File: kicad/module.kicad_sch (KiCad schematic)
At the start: 14 parts, among them J2 Conn_01x12, J3 Conn_01x10, J4 Conn_01x02, Q1 SI2302CDS, SW1 CNK_KMR2, U10 RioteeModule, U9 TS5A3166YZP

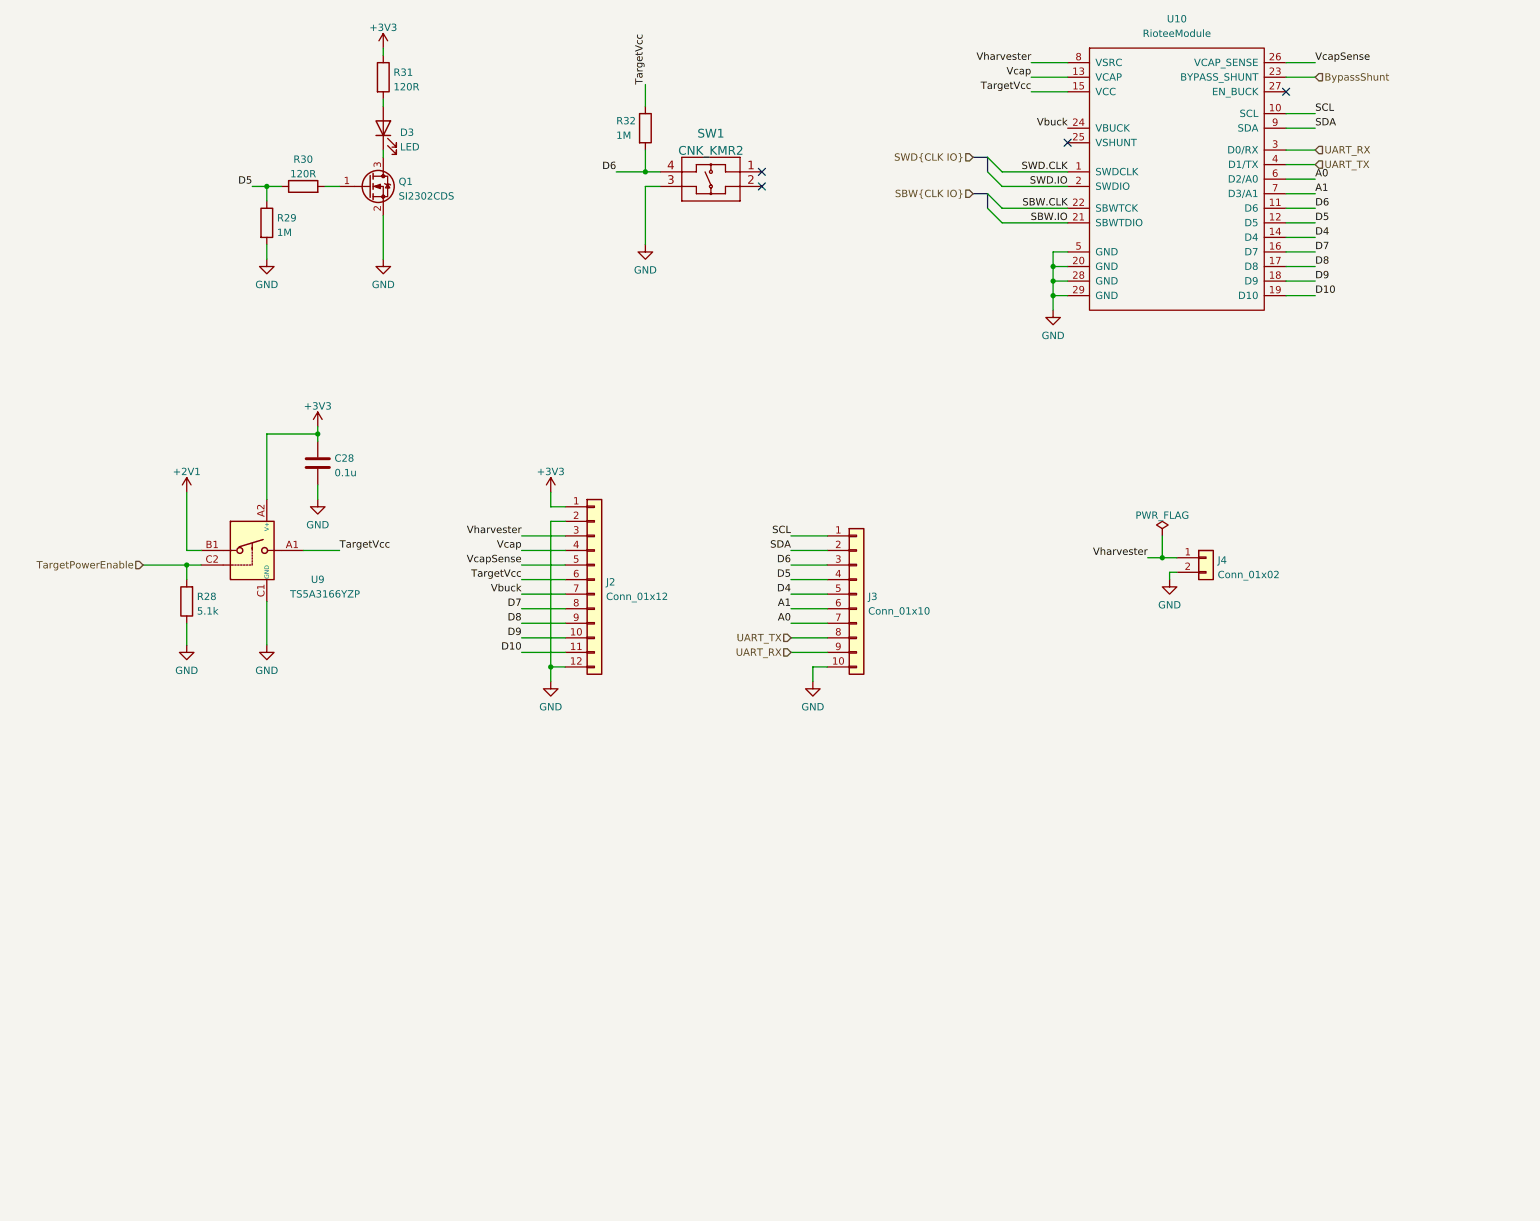
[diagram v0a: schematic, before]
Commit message: copy in module schematics
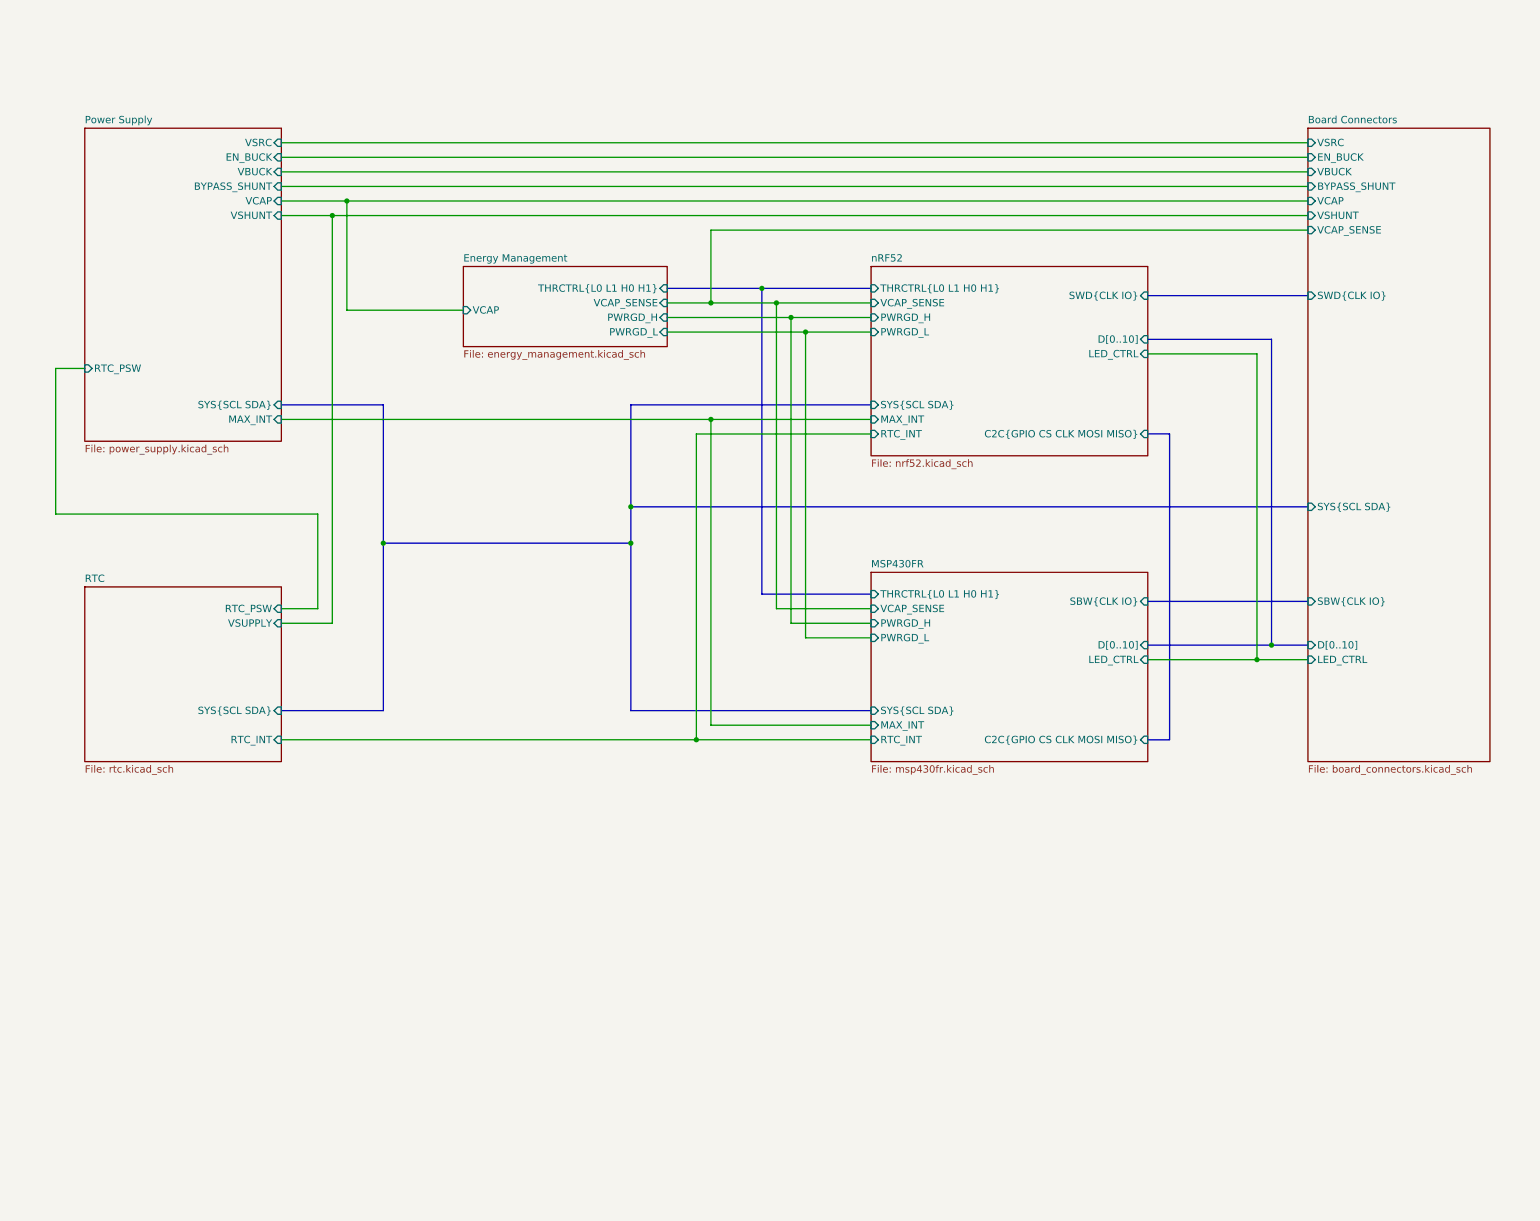
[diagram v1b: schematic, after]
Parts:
- removed C28: 0.1u, Capacitor_SMD:C_0402_1005Metric, symbol Device:C
- removed D3: LED, LED_SMD:LED_0402_1005Metric, symbol Device:LED
- removed J2: Conn_01x12, riotee:PinSocket_1x12_P2.54mm_Vertical, symbol Connector_Generic:Conn_01x12
- removed J3: Conn_01x10, riotee:PinSocket_1x10_P2.54mm_Vertical, symbol Connector_Generic:Conn_01x10
- removed J4: Conn_01x02, riotee:JST_S2B-PH-SM4-TB(LF)(SN), symbol Connector_Generic:Conn_01x02
- removed Q1: SI2302CDS, riotee:VSH_SOT-23-3, symbol riotee:SI2302CDS
- removed R28: 5.1k, Resistor_SMD:R_0402_1005Metric, symbol Device:R
- removed R29, R32: 1M, Resistor_SMD:R_0402_1005Metric, symbol Device:R
- removed R30, R31: 120R, Resistor_SMD:R_0402_1005Metric, symbol Device:R
- removed SW1: CNK_KMR2, riotee:CNK_KMR2_SW, symbol riotee:CNK_KMR2
- removed U10: RioteeModule, riotee:NC_RioteeModule, symbol riotee:RioteeModule
- removed U9: TS5A3166YZP, riotee:TI_YZP0005, symbol riotee:TS5A3166YZP
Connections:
- no-connect marks 4 -> 0
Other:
- added sheet Board Connectors (board_connectors.kicad_sch)
- added sheet Energy Management (energy_management.kicad_sch)
- added sheet MSP430FR (msp430fr.kicad_sch)
- added sheet Power Supply (power_supply.kicad_sch)
- added sheet RTC (rtc.kicad_sch)
- added sheet nRF52 (nrf52.kicad_sch)

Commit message: unify module and board
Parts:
- added D4: LED, Riotee:LED_0402_1005Metric, symbol Riotee:LED
- added J5: RFShield_OnePiece, Riotee:EMI_SHIELD_CSTM, symbol Device:RFShield_OnePiece
- added Q2: PMCM4401VNE, Riotee:NXP_WLCSP4, symbol Riotee:PMCM4401VNE
- added R33: 220k, Riotee:R_0201_0603Metric, symbol Riotee:R
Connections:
- new net: D4.1 (K), Q2.B1 (D)
- new net GND: J5.1 (Shield), Q2.A2 (S), R33.2
- new net LED_CTRL: Q2.A1 (G), R33.1
- new net VCC: D4.2 (A)
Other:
- removed sheet Board Connectors

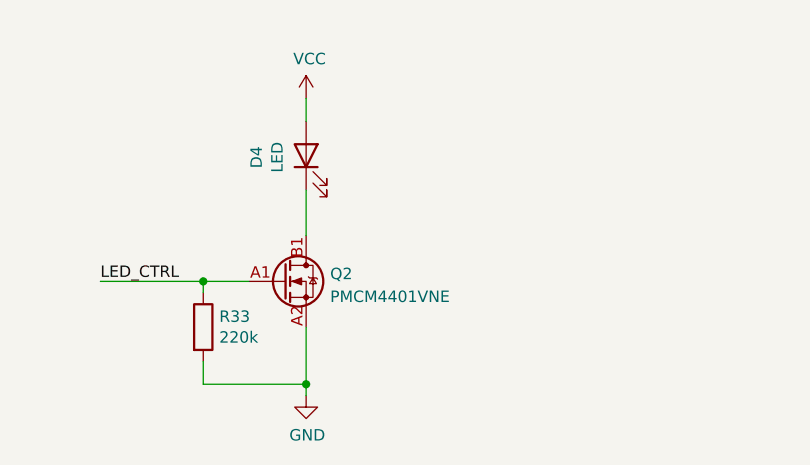
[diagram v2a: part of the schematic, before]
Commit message: move module parts to common library
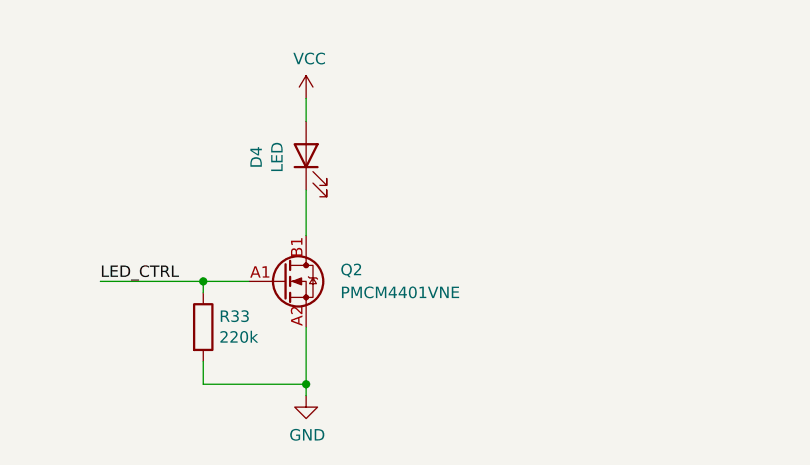
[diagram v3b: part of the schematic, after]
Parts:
- Q2: symbol Riotee:PMCM4401VNE -> riotee:PMCM4401VNE
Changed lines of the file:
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@@
 	)
 	(symbol
-		(lib_id "Riotee:PMCM4401VNE")
+		(lib_id "riotee:PMCM4401VNE")
 		(at 205.74 214.63 0)
 		(unit 1)
@@
 		(fields_autoplaced yes)
 		(property "Reference" "Q2"
-			(at 210.947 213.7953 0)
+			(at 212.09 213.3599 0)
 			(effects
 				(font
@@
 		)
 		(property "Value" "PMCM4401VNE"
-			(at 210.947 216.3322 0)
+			(at 212.09 215.8999 0)
 			(effects
 				(font
@@
 			)
 		)
-		(property "Description" "MOSFET N-CH 12V 4.7A 4WLCSP"
+		(property "Description" "N-MOSFET transistor"
 			(at 205.74 214.63 0)
 			(effects

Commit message: resolve ERC
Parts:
- D4: footprint Riotee:LED_0402_1005Metric -> riotee:LED_0402_1005Metric; symbol Riotee:LED -> Device:LED
- J5: footprint Riotee:EMI_SHIELD_CSTM -> riotee:EMI_SHIELD_CSTM
- Q2: footprint Riotee:NXP_WLCSP4 -> riotee:NXP_WLCSP4
- R33: footprint Riotee:R_0201_0603Metric -> riotee:R_0201_0603Metric; symbol Riotee:R -> Device:R
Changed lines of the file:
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@@
 	)
 	(symbol
-		(lib_id "Riotee:R")
+		(lib_id "Device:R")
 		(at 196.85 219.71 0)
 		(unit 1)
@@
 			)
 		)
-		(property "Footprint" "Riotee:R_0201_0603Metric"
+		(property "Footprint" "riotee:R_0201_0603Metric"
 			(at 195.072 219.71 90)
 			(effects
@@
 			)
 		)
-		(property "Description" "RES SMD 220K OHM 1% 1/20W 0201"
+		(property "Description" "Resistor"
 			(at 196.85 219.71 0)
 			(effects
@@
 	)
 	(symbol
-		(lib_id "Riotee:GND")
+		(lib_id "power:GND")
 		(at 124.46 223.52 0)
 		(unit 1)
@@
 			)
 		)
-		(property "Description" ""
+		(property "Description" "Power symbol creates a global label with name \"GND\" , ground"
 			(at 124.46 223.52 0)
 			(effects
@@
 			)
 		)
-		(property "Footprint" "Riotee:NXP_WLCSP4"
+		(property "Footprint" "riotee:NXP_WLCSP4"
 			(at 205.74 229.87 0)
 			(effects
@@
 	)
 	(symbol
-		(lib_id "Riotee:GND")
+		(lib_id "power:GND")
 		(at 208.28 227.33 0)
 		(unit 1)
@@
 			)
 		)
-		(property "Description" ""
+		(property "Description" "Power symbol creates a global label with name \"GND\" , ground"
 			(at 208.28 227.33 0)
 			(effects
@@
 			)
 		)
-		(property "Footprint" "Riotee:EMI_SHIELD_CSTM"
+		(property "Footprint" "riotee:EMI_SHIELD_CSTM"
 			(at 124.46 213.36 0)
 			(effects
@@
 	)
 	(symbol
-		(lib_id "Riotee:LED")
+		(lib_id "Device:LED")
 		(at 208.28 200.66 90)
 		(unit 1)
@@
 			)
 		)
-		(property "Footprint" "Riotee:LED_0402_1005Metric"
+		(property "Footprint" "riotee:LED_0402_1005Metric"
 			(at 208.28 200.66 0)
 			(effects
@@
 			)
 		)
-		(property "Description" "SMD LED 0402 RED 625NM"
+		(property "Description" "Light emitting diode"
 			(at 208.28 200.66 0)
 			(effects
@@
 			(at 208.28 200.66 0)
 			(effects
+				(font
+					(size 1.27 1.27)
+				)
+				(hide yes)
+			)
+		)
+		(property "Sim.Pins" "1=K 2=A"
+			(at 208.28 200.66 0)
+			(effects

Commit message: resolve remaining import errors
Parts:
- D4: footprint riotee:LED_0402_1005Metric -> LED_SMD:LED_0402_1005Metric
- J5: footprint riotee:EMI_SHIELD_CSTM -> riotee:MS209-20F
- R33: footprint riotee:R_0201_0603Metric -> Resistor_SMD:R_0201_0603Metric
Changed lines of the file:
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@@
 			)
 		)
-		(property "Footprint" "riotee:R_0201_0603Metric"
+		(property "Footprint" "Resistor_SMD:R_0201_0603Metric"
 			(at 195.072 219.71 90)
 			(effects
@@
 			)
 		)
-		(property "Footprint" "riotee:EMI_SHIELD_CSTM"
+		(property "Footprint" "riotee:MS209-20F"
 			(at 124.46 213.36 0)
 			(effects
@@
 			)
 		)
-		(property "Footprint" "riotee:LED_0402_1005Metric"
+		(property "Footprint" "LED_SMD:LED_0402_1005Metric"
 			(at 208.28 200.66 0)
 			(effects

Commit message: pcb: update mpn of wlcsp transistors
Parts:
- Q2: MPN PMCM4401VNEAZ -> PMCM4401UNEZ
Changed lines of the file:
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@@
 			)
 		)
-		(property "MPN" "PMCM4401VNEAZ"
+		(property "MPN" "PMCM4401UNEZ"
 			(at 205.74 214.63 0)
 			(effects
